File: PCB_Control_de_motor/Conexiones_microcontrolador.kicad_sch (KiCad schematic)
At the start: 20 parts, among them IC1 ESP32-S3-WROOM-1-N16, IC2 USBLC6-2SC6, SW1 SSSF021500

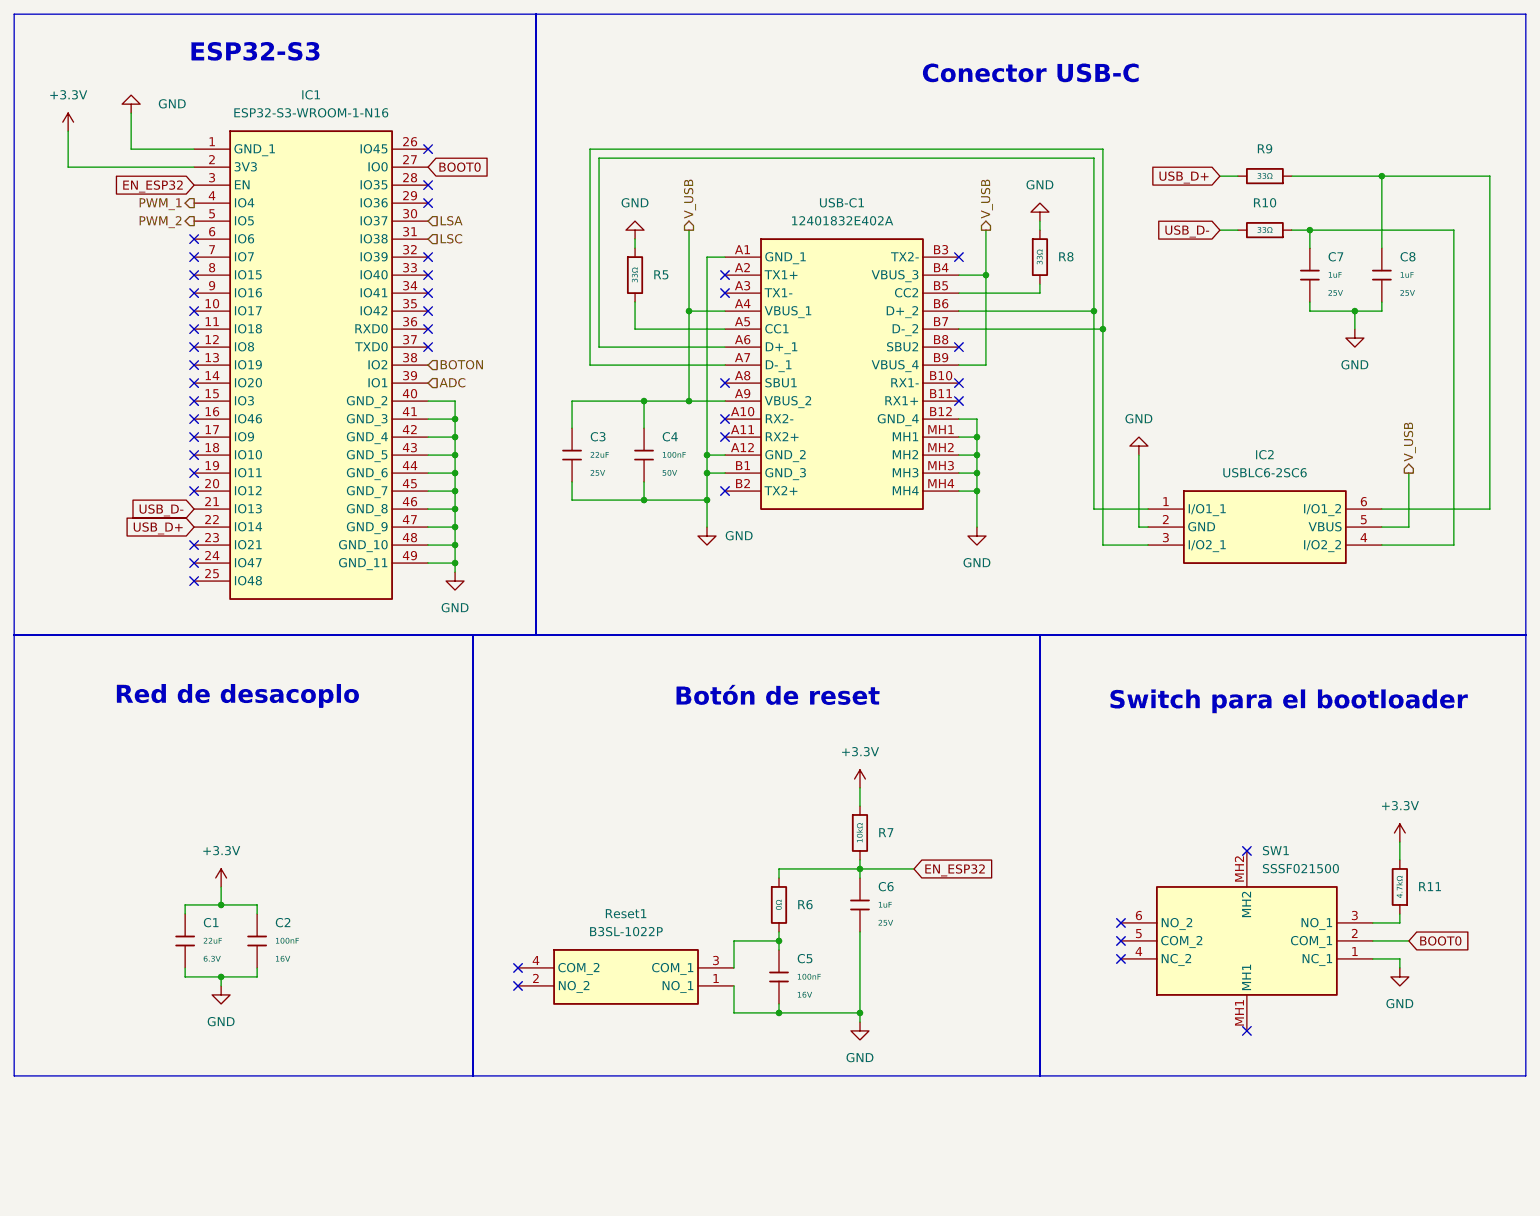
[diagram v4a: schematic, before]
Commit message: Agregado de diodos TVS y avance del PCB con fuente y micro listo
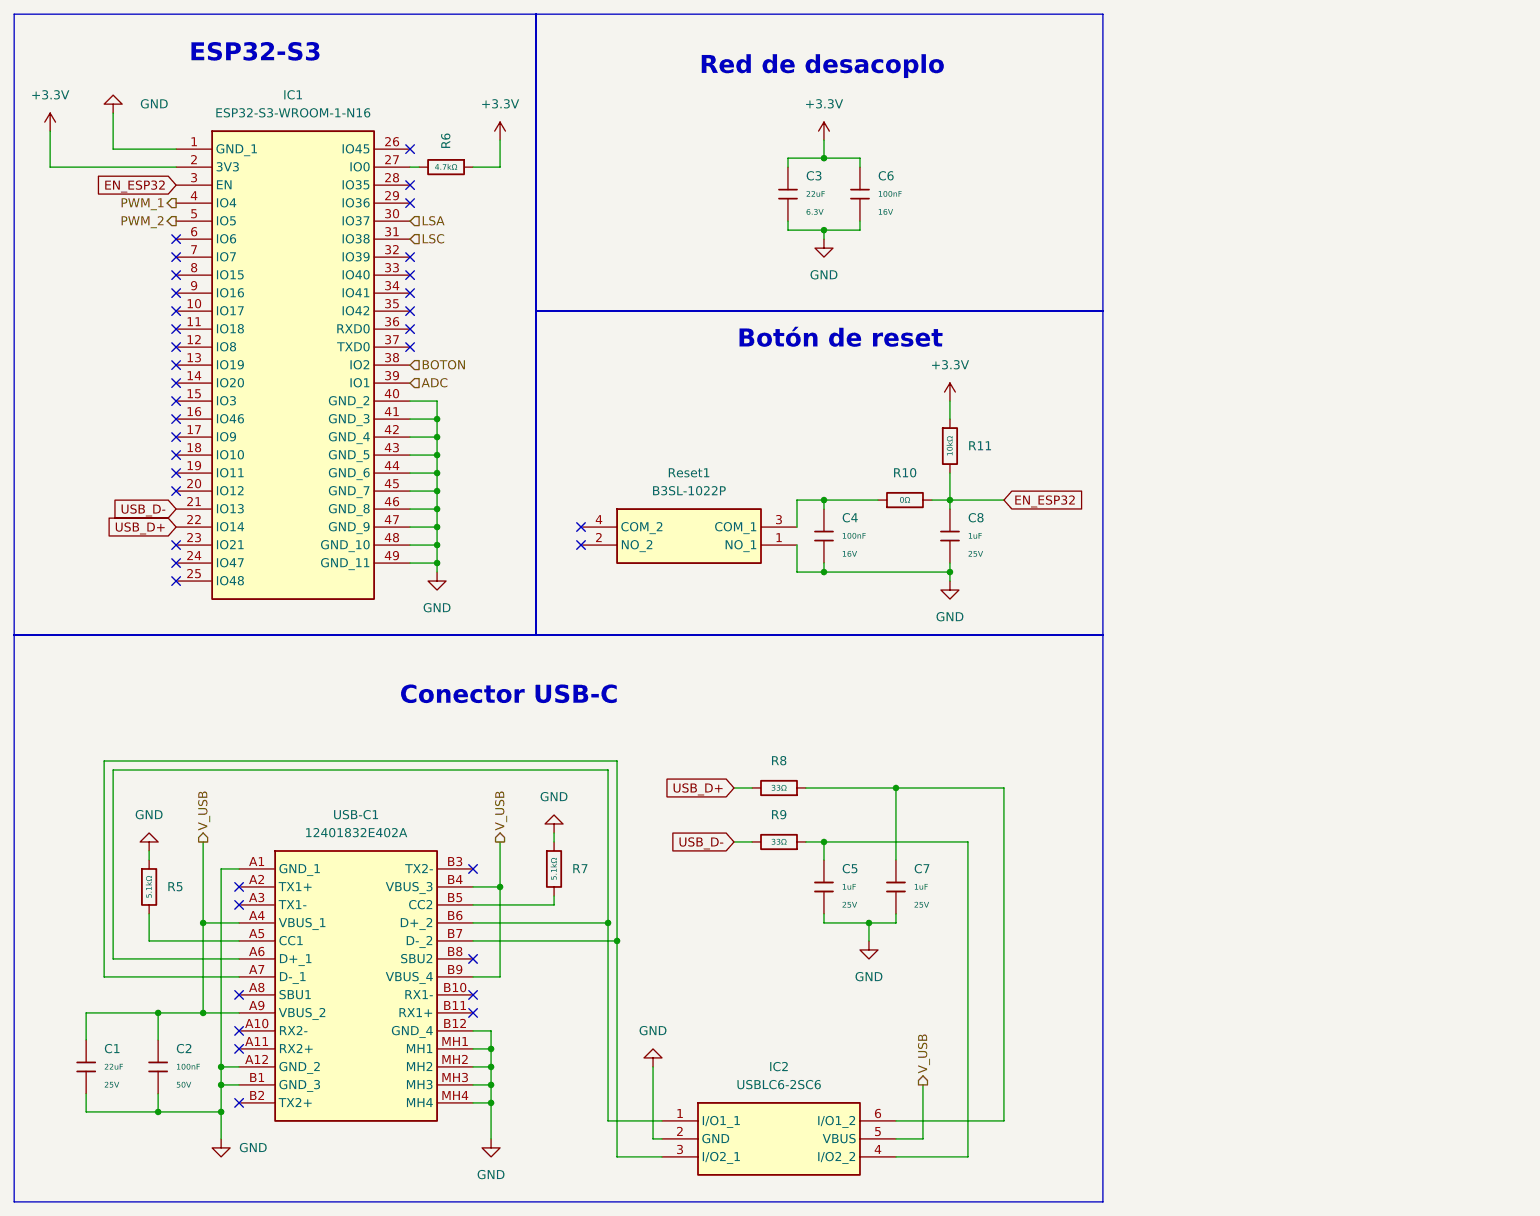
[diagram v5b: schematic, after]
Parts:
- removed R5, R8: 33Ω, PCM_JLCPCB:R_0603, symbol PCM_JLCPCB-Resistors:0603,33Ω
- removed SW1: SSSF021500, SamacSys_Parts:SSSF021500, symbol SamacSys_Parts:SSSF021500
- added R5, R7: 5.1kΩ, PCM_JLCPCB:R_0805, symbol PCM_JLCPCB-Resistors:0805,5.1kΩ
- renumbered C3 to C1, C4 to C2, C1 to C3, C5 to C4, C7 to C5, C2 to C6, C8 to C7, C6 to C8, R6 to R10, R7 to R11, R11 to R6, R9 to R8, R10 to R9
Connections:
- net +3.3V: now also R6.1; no longer R6.2
- net EN_ESP32: now also R10.2; no longer R10.1
- net GND: now also R5.1, R7.1
- net at USB-C1.A5 (CC1): now also R5.2
- net at C4.1, Reset1.3 (COM_1): now also R10.1; no longer R10.2
- net at USB-C1.B5 (CC2): now also R7.2
- net BOOT0: no longer names the net of IC1.27 (IO0)
- net BOOT0: now also R6.2
- no-connect marks 44 -> 39
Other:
- note removed: "Switch para el bootloader"
- moved on the sheet: C1, C2, C3, C4, C5, C6, C7, C8, IC1, IC2, R10, R11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
